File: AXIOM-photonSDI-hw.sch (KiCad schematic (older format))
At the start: 4 parts, among them J101 Conn_Coaxial, J102 Conn_Coaxial, J103 Conn_Coaxial, J104 Conn_Coaxial

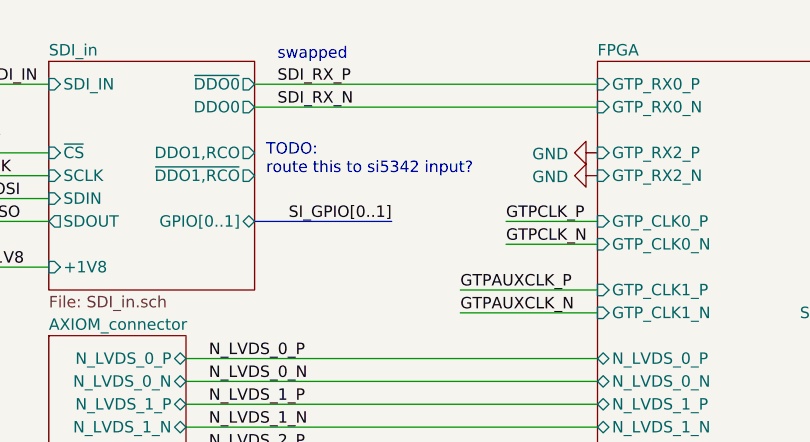
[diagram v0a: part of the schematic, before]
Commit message: mark optional recovered clock output pins of GS12241 as unconnected
those outputs can't be easily routed to the inputs of the SI5342 chips, so I
don't support this on the hardware
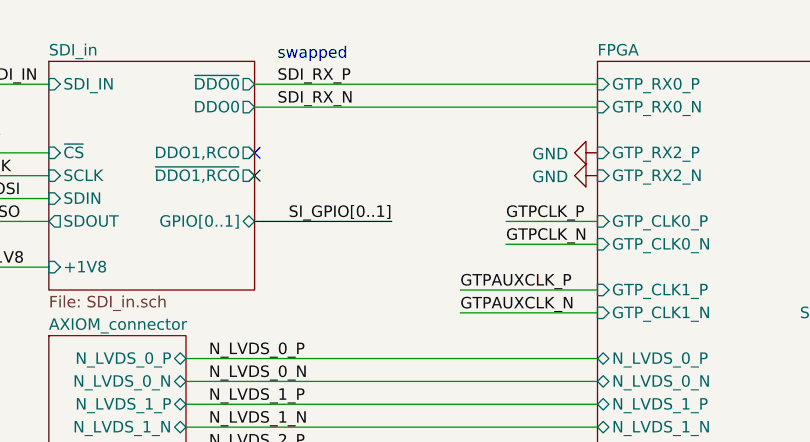
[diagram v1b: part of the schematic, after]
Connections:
- no-connect marks 0 -> 2
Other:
- note removed: "TODO:\nroute this to si5342 input?"
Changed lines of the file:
@@
 Text Label 2300 5700 0    50   ~ 0
 AUX1
-Text Notes 2550 1400 0    50   ~ 0
-TODO:\nroute this to si5342 input?
 $Comp
 L power:GND #PWR0104
@@
 Text Label 2700 6700 2    50   ~ 0
 HSYNC12
+NoConn ~ 2500 1300
+NoConn ~ 2500 1400
 $EndSCHEMATC

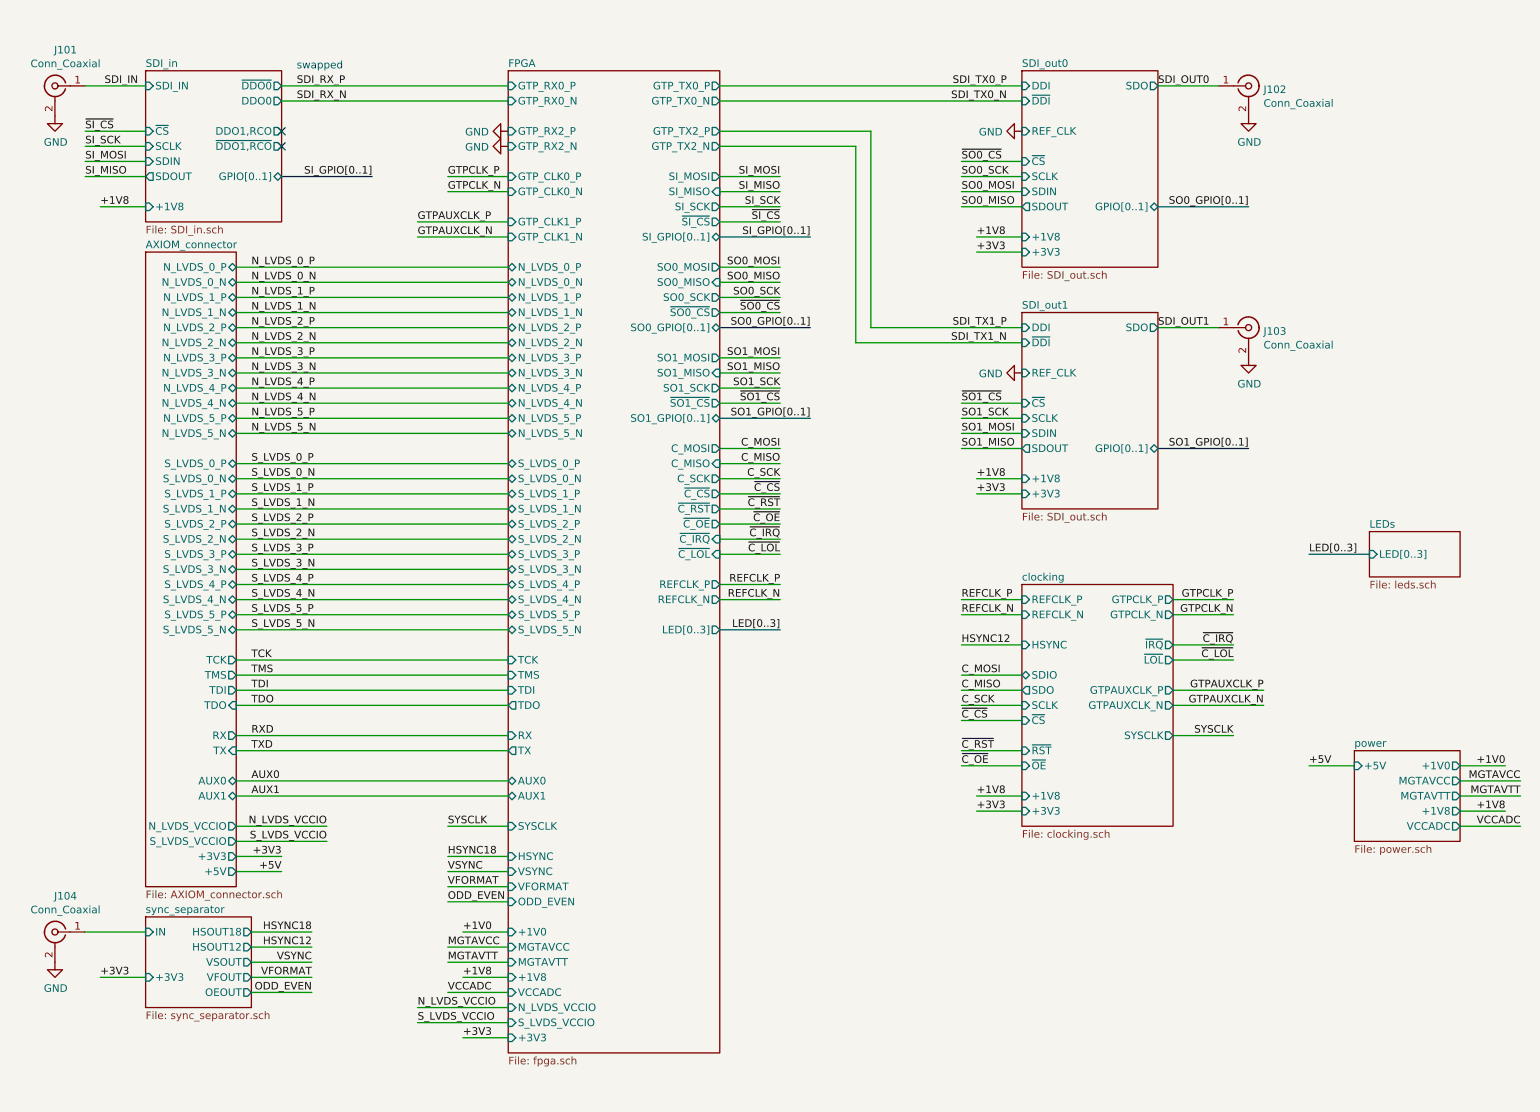
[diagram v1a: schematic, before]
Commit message: remove crystal oscillator from second GTP clock input pair
The oscillator was intended as a workaround for possible problems with the
clock from the SI5342, but was rather difficult to fit on the PCB without
having to compromise on other aspects.
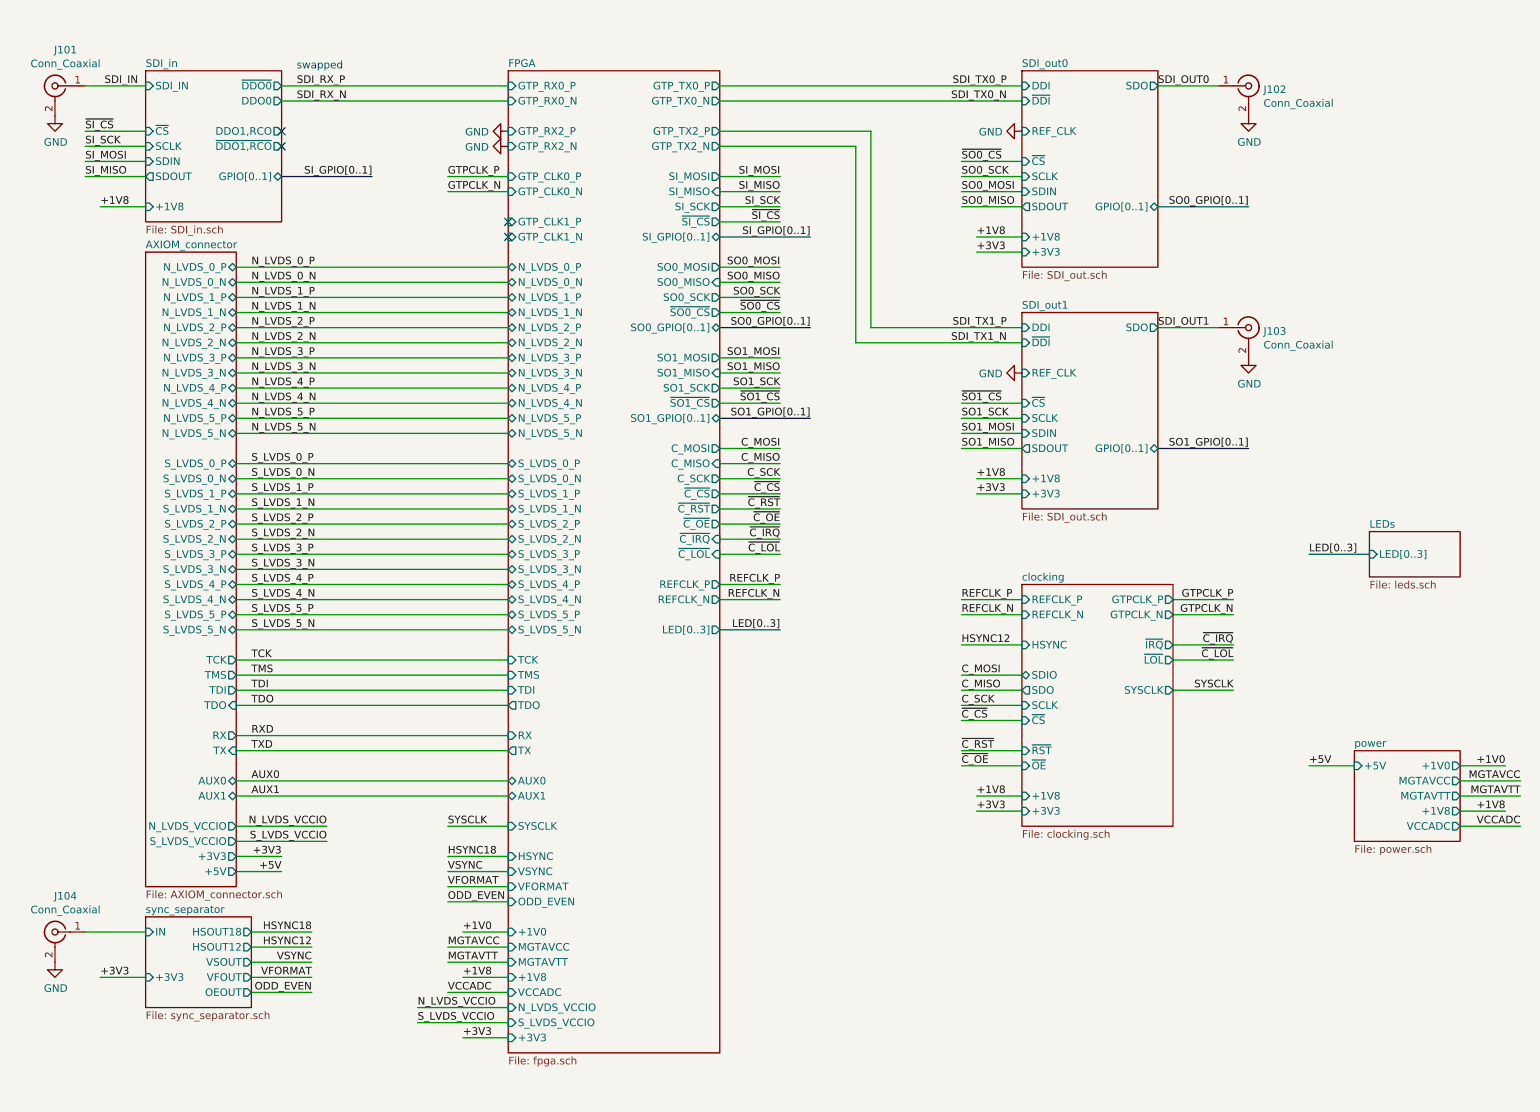
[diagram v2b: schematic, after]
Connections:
- no-connect marks 2 -> 4
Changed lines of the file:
@@
 F10 "+1V8" I L 7400 5700 50
 F11 "+3V3" I L 7400 5800 50
-F12 "SYSCLK" O R 8400 5300 50
-F13 "GTPAUXCLK_P" O R 8400 5000 50
-F14 "GTPAUXCLK_N" O R 8400 5100 50
-F15 "HSYNC" I L 7400 4700 50
-F16 "~RST" I L 7400 5400 50
-F17 "~OE" I L 7400 5500 50
-F18 "~IRQ" O R 8400 4700 50
-F19 "~LOL" O R 8400 4800 50
+F12 "SYSCLK" O R 8400 5000 50
+F13 "HSYNC" I L 7400 4700 50
+F14 "~RST" I L 7400 5400 50
+F15 "~OE" I L 7400 5500 50
+F16 "~IRQ" O R 8400 4700 50
+F17 "~LOL" O R 8400 4800 50
 $EndSheet
 $Sheet
@@
 SYSCLK
 Wire Wire Line
-	8800 5300 8400 5300
-Text Label 8800 5300 2    50   ~ 0
+	8800 5000 8400 5000
+Text Label 8800 5000 2    50   ~ 0
 SYSCLK
 Wire Wire Line
@@
 REFCLK_N
 Wire Wire Line
-	9000 5000 8400 5000
-Wire Wire Line
-	9000 5100 8400 5100
-Text Label 9000 5000 2    50   ~ 0
-GTPAUXCLK_P
-Text Label 9000 5100 2    50   ~ 0
-GTPAUXCLK_N
-Wire Wire Line
 	3600 1600 4000 1600
 Wire Wire Line
@@
 Text Label 3600 1700 0    50   ~ 0
 GTPCLK_N
-Wire Wire Line
-	3400 1900 4000 1900
-Wire Wire Line
-	3400 2000 4000 2000
-Text Label 3400 1900 0    50   ~ 0
-GTPAUXCLK_P
-Text Label 3400 2000 0    50   ~ 0
-GTPAUXCLK_N
 Wire Bus Line
 	5400 4600 5800 4600
@@
 NoConn ~ 2500 1300
 NoConn ~ 2500 1400
+NoConn ~ 4000 1900
+NoConn ~ 4000 2000
 $EndSCHEMATC

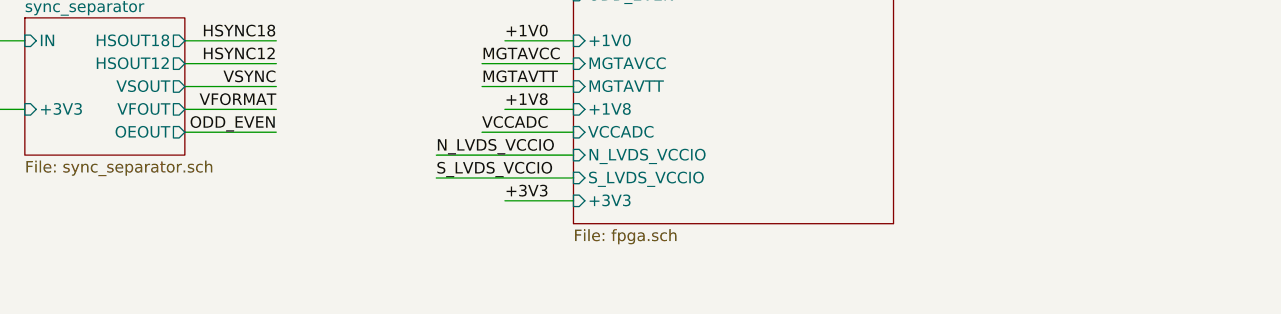
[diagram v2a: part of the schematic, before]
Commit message: specify voltage rating of capacitors
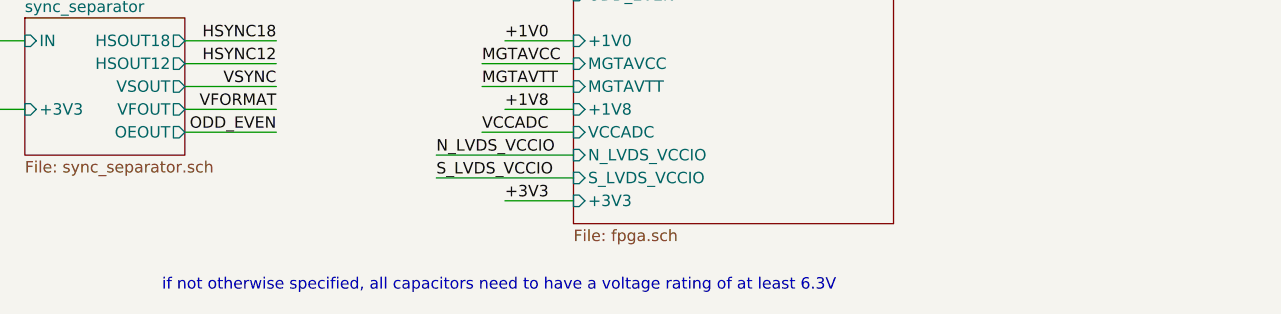
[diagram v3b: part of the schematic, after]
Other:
- note added: "if not otherwise specified, all capacitors need to have a voltage rating of at least 6.3V"
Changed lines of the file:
@@
 NoConn ~ 4000 1900
 NoConn ~ 4000 2000
+Text Notes 2200 7700 0    50   ~ 0
+if not otherwise specified, all capacitors need to have a voltage rating of at least 6.3V
 $EndSCHEMATC

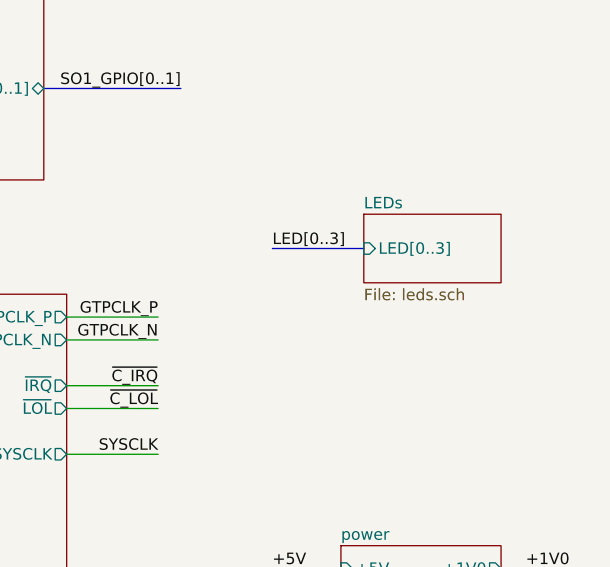
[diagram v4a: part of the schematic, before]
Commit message: connect the non-fpga pin of the leds to vcc insted of gnd
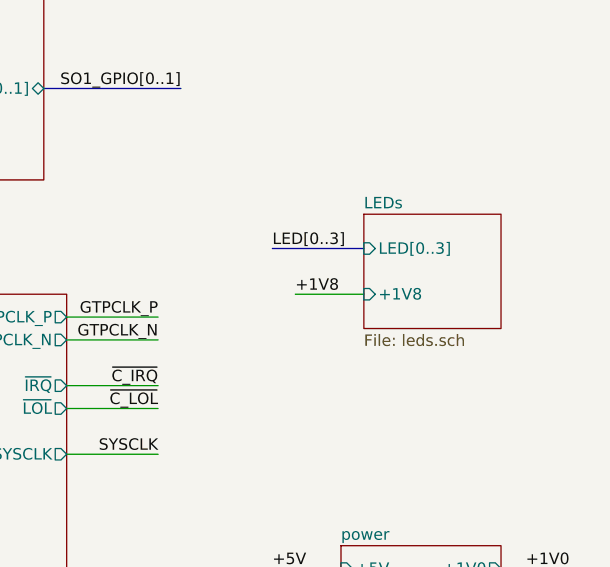
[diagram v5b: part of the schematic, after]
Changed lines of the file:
@@
 SDI_IN
 $Sheet
-S 9700 3950 600  300
+S 9700 3950 600  500
 U 5AFE2BD2
 F0 "LEDs" 50
 F1 "leds.sch" 50
 F2 "LED[0..3]" I L 9700 4100 50
+F3 "+1V8" I L 9700 4300 50
 $EndSheet
 $Sheet
@@
 Text Notes 2200 7700 0    50   ~ 0
 if not otherwise specified, all capacitors need to have a voltage rating of at least 6.3V
+Wire Wire Line
+	9400 4300 9700 4300
+Text Label 9400 4300 0    50   ~ 0
++1V8
 $EndSCHEMATC

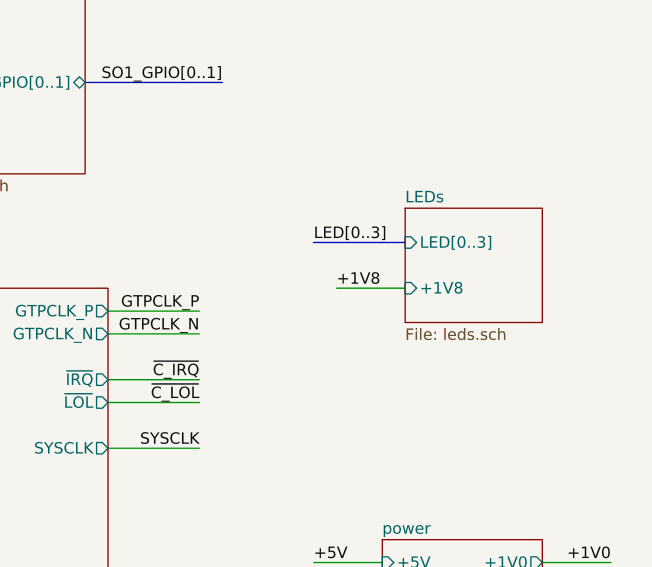
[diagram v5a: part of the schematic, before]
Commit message: connect leds to 3v3 power supply rail
the led is still connected to a 1v8 fpga io bank though
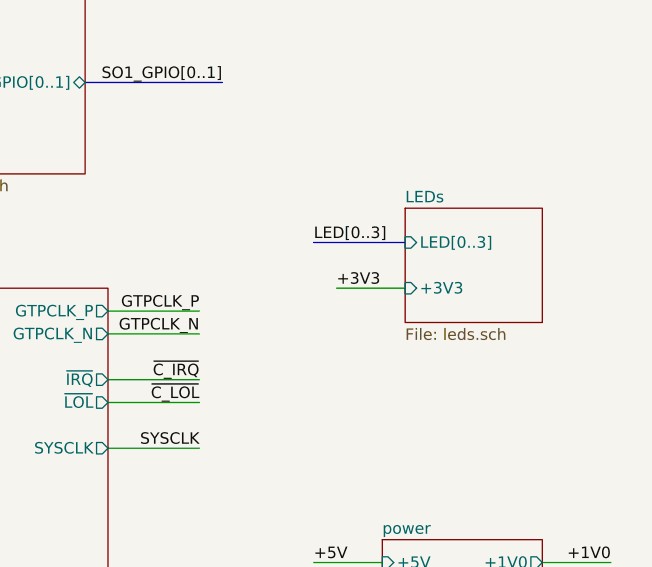
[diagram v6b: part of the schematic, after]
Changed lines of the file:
@@
 F1 "leds.sch" 50
 F2 "LED[0..3]" I L 9700 4100 50
-F3 "+1V8" I L 9700 4300 50
+F3 "+3V3" I L 9700 4300 50
 $EndSheet
 $Sheet
@@
 	9400 4300 9700 4300
 Text Label 9400 4300 0    50   ~ 0
-+1V8
++3V3
 $EndSCHEMATC
